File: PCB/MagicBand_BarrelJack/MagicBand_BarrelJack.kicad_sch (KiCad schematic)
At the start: 18 parts, among them J2 MFRC522_Module, J3 RF_TX_DFLIFE, J6 NeoPixel_Outer_16px, J7 NeoPixel_Inner_12px, J8 DC_Barrel_Jack_5.5x2.1mm, J9 ISP_AVR_2x3, U1 ATmega328P-P, U2 MCP1700-3302, Y1 16MHz

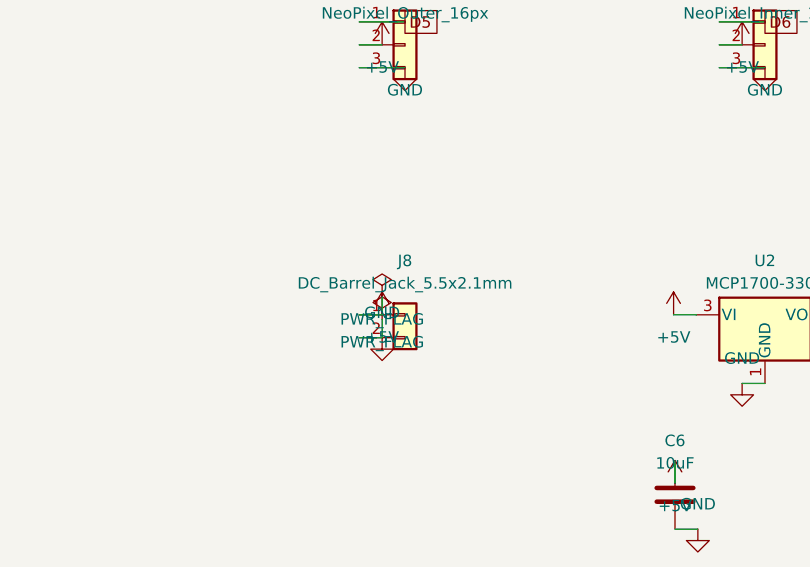
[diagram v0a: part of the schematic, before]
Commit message: Document front/back layout constraint, relabel barrel jack connector
RFID+MCU stack must sit at the front (interactive/tap end) of the
ornament; the barrel jack must be at the back. The jack itself is a
separate panel-mount part with bare flying leads, not board-mounted --
it connects to the board via two soldered wires, not a purchased
connector. Relabeled J8 to PWR_IN_BarrelJack_BareLeads to make that
explicit, and added a Physical Layout Constraint section to the PCB
Design Plan so this isn't missed once actual placement/routing starts.
ERC re-run clean, no regression.

Co-Authored-By: Claude Sonnet 5 <noreply@anthropic.com>
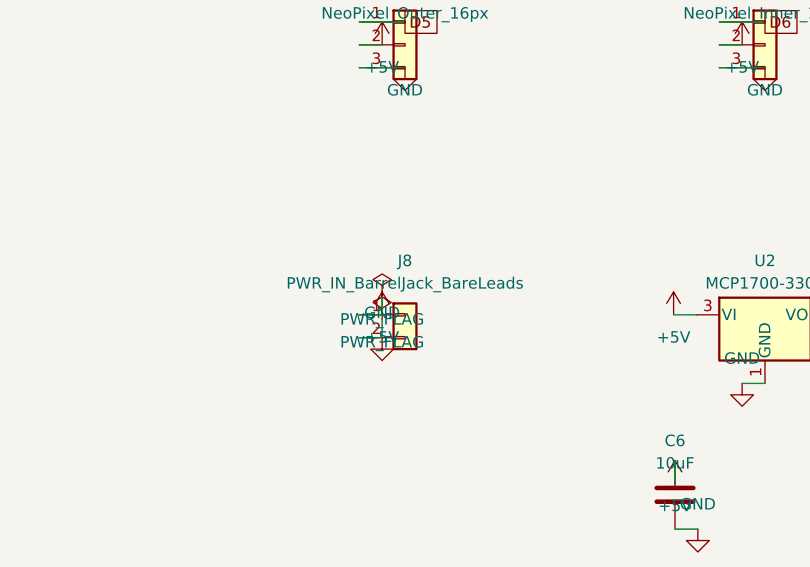
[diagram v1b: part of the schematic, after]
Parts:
- J8: value DC_Barrel_Jack_5.5x2.1mm -> PWR_IN_BarrelJack_BareLeads
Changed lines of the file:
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@@
 			(effects (font (size 1.27 1.27)))
 		)
-		(property "Value" "DC_Barrel_Jack_5.5x2.1mm"
+		(property "Value" "PWR_IN_BarrelJack_BareLeads"
 			(at 250 126.5 0)
 			(effects (font (size 1.27 1.27)))

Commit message: NeoPixel headers: JST-PH connector, pin order documented
J6/J7 changed from generic 2.54mm pin headers to JST-PH 3-pin connectors
for easier connect/disconnect at assembly. Pin order (1=DATA, 2=+5V,
3=GND) confirmed identical on both headers via netlist before the swap,
and documented in PCB Design Plan.md since there's no external standard
JST pin order for WS2812 strips to rely on -- the user is terminating
both ends themselves, so this table is the source of truth.

J3 (RF TX module) shares the same generic footprint family and was
deliberately left untouched -- caught by an assertion check before the
replacement ran, not something that would have been obvious from a
find-and-replace alone.

ERC re-run clean, no regression (0 errors, 194 warnings).

Co-Authored-By: Claude Sonnet 5 <noreply@anthropic.com>
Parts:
- J6, J7: footprint Connector_PinHeader_2.54mm:PinHeader_1x03_P2.54mm_Vertical -> Connector_JST:JST_PH_B3B-PH-K_1x03_P2.00mm_Vertical
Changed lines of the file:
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@@
 			(effects (font (size 1.27 1.27)))
 		)
-		(property "Footprint" "Connector_PinHeader_2.54mm:PinHeader_1x03_P2.54mm_Vertical"
+		(property "Footprint" "Connector_JST:JST_PH_B3B-PH-K_1x03_P2.00mm_Vertical"
 			(at 250 100 0)
 			(effects (font (size 1.27 1.27)) (hide yes))
@@
 			(effects (font (size 1.27 1.27)))
 		)
-		(property "Footprint" "Connector_PinHeader_2.54mm:PinHeader_1x03_P2.54mm_Vertical"
+		(property "Footprint" "Connector_JST:JST_PH_B3B-PH-K_1x03_P2.00mm_Vertical"
 			(at 290 100 0)
 			(effects (font (size 1.27 1.27)) (hide yes))

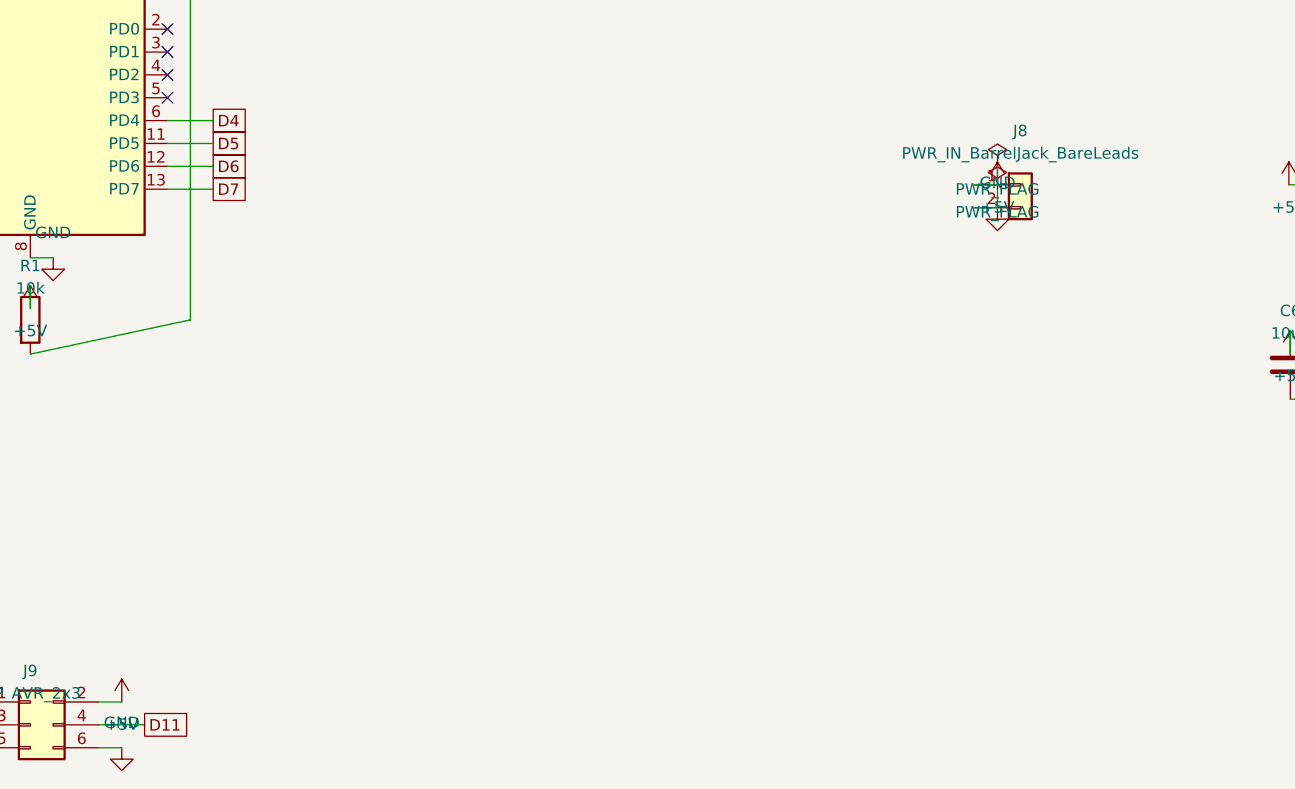
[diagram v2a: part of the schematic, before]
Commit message: Close PDR gaps: reverse-polarity protection, firmware trim, cleanup
Adversarial PDR found one blocking issue and five should-fix items on
PCB/MagicBand_BarrelJack/MagicBand_BarrelJack.kicad_sch. All closed:

- Blocking: added a P-channel MOSFET (Q1, AO3401A) ideal-diode
  reverse-polarity protection circuit ahead of the regulator/MCU -- the
  barrel jack is bare wire leads with no mechanical keying, a real risk
  of a reversed or wrong-voltage adapter with nothing previously in the
  way. MOSFET chosen over a simple diode to avoid eating into the
  ATmega328P's 16MHz voltage headroom. Topology cross-checked against
  real references before committing. ERC-clean (0 errors, 209 warnings)
  after fixing real geometry/connectivity issues hit while authoring it.

- Should-fix: removed an orphaned D7 label (explicit no-connect added),
  linked the front/back layout constraint into the WP4.1 task text,
  documented the MFRC522/ISP shared-SPI-bus gotcha, made the MCP1700-keep
  decision explicit, fixed a doc typo (SOT-23-5 -> SOT-23).

- Firmware: new MagicBand_BarrelJack.ino, derived from
  MagicBand_Wireless.ino with the sleep/wake watchdog loop and MOSFET
  gating calls removed -- the leftover ~1s poll delay was a real UX
  regression, not just stale code. Compiles clean.

Co-Authored-By: Claude Sonnet 5 <noreply@anthropic.com>
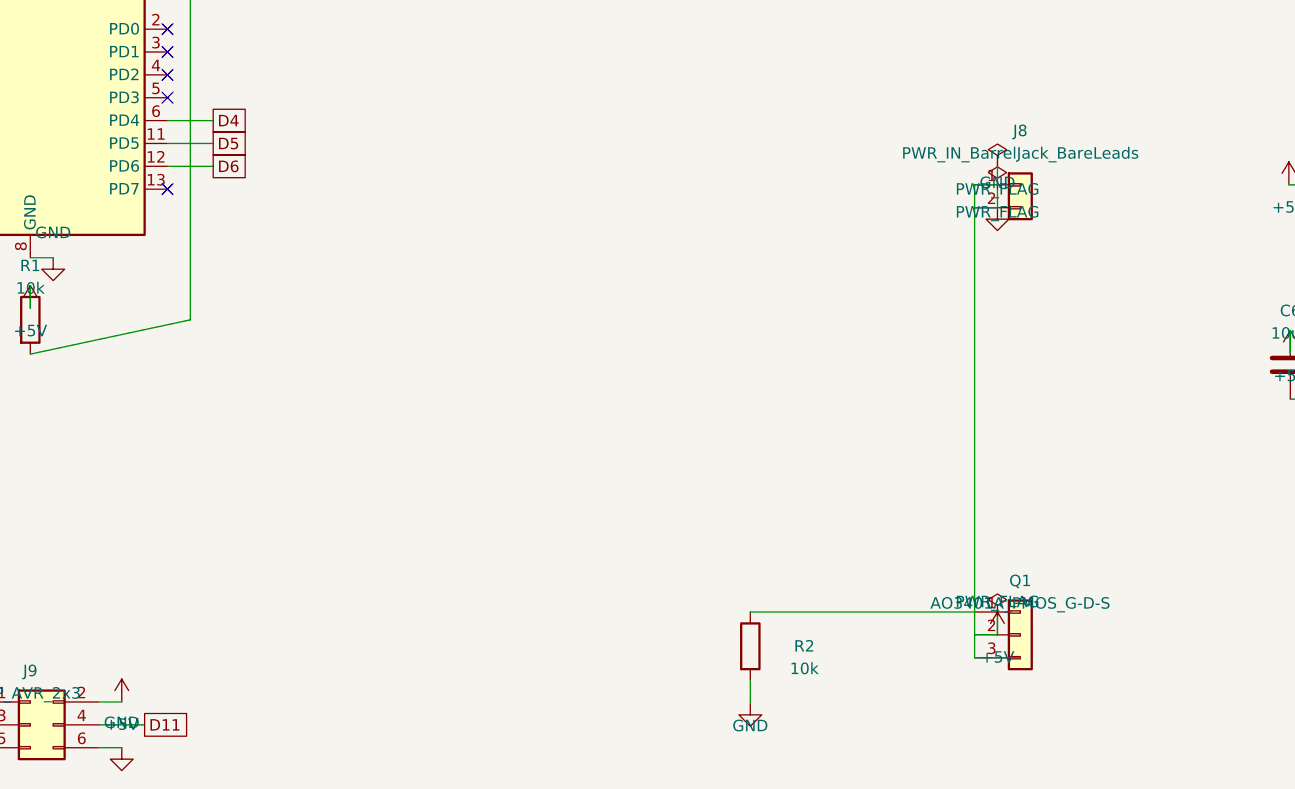
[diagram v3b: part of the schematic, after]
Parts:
- added Q1: AO3401A_PMOS_G-D-S, Package_TO_SOT_SMD:SOT-23, symbol Connector_Generic:Conn_01x03
- added R2: 10k, Resistor_THT:R_Axial_DIN0207_L6.3mm_D2.5mm_P10.16mm_Horizontal, symbol Device:R
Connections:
- net +5V: now also Q1.2 (Pin_2); no longer J8.1 (Pin_1)
- net GND: now also R2.2
- net D7: no longer names the net of U1.13 (PD7)
- new net: J8.1 (Pin_1), Q1.3 (Pin_3)
- new net: Q1.1 (Pin_1), R2.1
- no-connect marks 12 -> 13
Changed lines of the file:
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@@
-	)
-	(wire
-		(pts (xy 155.24 130.48) (xy 160.32 130.48))
-		(stroke (width 0) (type default))
-	)
-	(global_label "D7"
-		(shape passive)
-		(at 160.32 130.48 0)
-		(fields_autoplaced yes)
-		(effects (font (size 1.27 1.27)) (justify left))
 	)
 	(wire
@@
 	(no_connect (at 155.24 120.32))
 	(no_connect (at 155.24 74.6))
+	(no_connect (at 155.24 130.48))
 	(no_connect (at 155.24 92.38))
 	(no_connect (at 155.24 94.92))
@@
 	)
 	(wire
+		(pts (xy 244.92 130.0) (xy 244.92 182.54))
+		(stroke (width 0) (type default))
+	)
+	(wire
 		(pts (xy 244.92 130.0) (xy 247.45999999999998 130.0))
 		(stroke (width 0) (type default))
 	)
+	(wire
+		(pts (xy 244.92 182.54) (xy 250 182.54))
+		(stroke (width 0) (type default))
+	)
+	(symbol
+		(lib_id "Connector_Generic:Conn_01x03")
+		(at 250 180 0)
+		(unit 1)
+		(exclude_from_sim no)
+		(in_bom yes)
+		(on_board yes)
+		(dnp no)
+		(property "Reference" "Q1"
+			(at 250 174 0)
+			(effects (font (size 1.27 1.27)))
+		)
+		(property "Value" "AO3401A_PMOS_G-D-S"
+			(at 250 176.5 0)
+			(effects (font (size 1.27 1.27)))
+		)
+		(property "Footprint" "Package_TO_SOT_SMD:SOT-23"
+			(at 250 180 0)
+			(effects (font (size 1.27 1.27)) (hide yes))
+		)
+		(property "Datasheet" ""
+			(at 250 180 0)
+			(effects (font (size 1.27 1.27)) (hide yes))
+		)
+		(pin "1")
+		(pin "2")
+		(pin "3")
+		(instances
+			(project "MagicBand_BarrelJack"
+				(path "/bcfef247-dfd6-4ae3-b42f-2bc22ccfcf8a"
+					(reference "Q1")
+					(unit 1)
+				)
+			)
+		)
+	)
+	(wire
+		(pts (xy 220 177.46) (xy 244.92 177.46))
+		(stroke (width 0) (type default))
+	)
+	(wire
+		(pts (xy 244.92 180.0) (xy 247.46 180.0))
+		(stroke (width 0) (type default))
+	)
 	(symbol
 		(lib_id "power:+5V")
-		(at 247.45999999999998 130.0 0)
-		(unit 1)
-		(exclude_from_sim no)
-		(in_bom yes)
-		(on_board yes)
-		(dnp no)
-		(property "Reference" "#PWR459d"
-			(at 247.45999999999998 126.5 0)
+		(at 247.46 180.0 0)
+		(unit 1)
+		(exclude_from_sim no)
+		(in_bom yes)
+		(on_board yes)
+		(dnp no)
+		(property "Reference" "#PWRQ1D"
+			(at 247.46 176.5 0)
 			(effects (font (size 1.27 1.27)) (hide yes))
 		)
 		(property "Value" "+5V"
-			(at 247.45999999999998 132.5 0)
-			(effects (font (size 1.27 1.27)))
-		)
-		(property "Footprint" ""
-			(at 247.45999999999998 130.0 0)
-			(effects (font (size 1.27 1.27)) (hide yes))
-		)
-		(property "Datasheet" ""
-			(at 247.45999999999998 130.0 0)
-			(effects (font (size 1.27 1.27)) (hide yes))
-		)
-		(pin "1")
-		(instances
-			(project "MagicBand_BarrelJack"
-				(path "/bcfef247-dfd6-4ae3-b42f-2bc22ccfcf8a"
-					(reference "#PWR459d")
-					(unit 1)
-				)
+			(at 247.46 182.5 0)
+			(effects (font (size 1.27 1.27)))
+		)
+		(property "Footprint" ""
+			(at 247.46 180.0 0)
+			(effects (font (size 1.27 1.27)) (hide yes))
+		)
+		(property "Datasheet" ""
+			(at 247.46 180.0 0)
+			(effects (font (size 1.27 1.27)) (hide yes))
+		)
+		(pin "1")
+		(instances
+			(project "MagicBand_BarrelJack"
+				(path "/bcfef247-dfd6-4ae3-b42f-2bc22ccfcf8a"
+					(reference "#PWRQ1D")
+					(unit 1)
+				)
+			)
+		)
+	)
+	(wire
+		(pts (xy 247.46 180.0) (xy 247.46 178.0))
+		(stroke (width 0) (type default))
+	)
+	(symbol
+		(lib_id "power:PWR_FLAG")
+		(at 247.46 178.0 0)
+		(unit 1)
+		(exclude_from_sim no)
+		(in_bom yes)
+		(on_board yes)
+		(dnp no)
+		(property "Reference" "#FLGQ1D"
+			(at 247.46 174.5 0)
+			(effects (font (size 1.27 1.27)) (hide yes))
+		)
+		(property "Value" "PWR_FLAG"
+			(at 247.46 176.34 0)
+			(effects (font (size 1.27 1.27)))
+		)
+		(property "Footprint" ""
+			(at 247.46 178.0 0)
+			(effects (font (size 1.27 1.27)) (hide yes))
+		)
+		(property "Datasheet" ""
+			(at 247.46 178.0 0)
+			(effects (font (size 1.27 1.27)) (hide yes))
+		)
+		(pin "1")
+		(instances
+			(project "MagicBand_BarrelJack"
+				(path "/bcfef247-dfd6-4ae3-b42f-2bc22ccfcf8a"
+					(reference "#FLGQ1D")
+					(unit 1)
+				)
+			)
+		)
+	)
+	(symbol
+		(lib_id "Device:R")
+		(at 220 181.27 0)
+		(unit 1)
+		(exclude_from_sim no)
+		(in_bom yes)
+		(on_board yes)
+		(dnp no)
+		(property "Reference" "R2"
+			(at 226 181.27 0)
+			(effects (font (size 1.27 1.27)))
+		)
+		(property "Value" "10k"
+			(at 226 183.77 0)
+			(effects (font (size 1.27 1.27)))
+		)
+		(property "Footprint" "Resistor_THT:R_Axial_DIN0207_L6.3mm_D2.5mm_P10.16mm_Horizontal"
+			(at 220 181.27 0)
+			(effects (font (size 1.27 1.27)) (hide yes))
+		)
+		(property "Datasheet" ""
+			(at 220 181.27 0)
+			(effects (font (size 1.27 1.27)) (hide yes))
+		)
+		(pin "1")
+		(pin "2")
+		(instances
+			(project "MagicBand_BarrelJack"
+				(path "/bcfef247-dfd6-4ae3-b42f-2bc22ccfcf8a"
+					(reference "R2")
+					(unit 1)
+				)
+			)
+		)
+	)
+	(wire
+		(pts (xy 220 185.08) (xy 220 187.62))
+		(stroke (width 0) (type default))
+	)
+	(symbol
+		(lib_id "power:GND")
+		(at 220 187.62 0)
+		(unit 1)
+		(exclude_from_sim no)
+		(in_bom yes)
+		(on_board yes)
+		(dnp no)
+		(property "Reference" "#PWRQ1G"
+			(at 220 184.12 0)
+			(effects (font (size 1.27 1.27)) (hide yes))
+		)
+		(property "Value" "GND"
+			(at 220 190.12 0)
+			(effects (font (size 1.27 1.27)))
+		)
+		(property "Footprint" ""
+			(at 220 187.62 0)
+			(effects (font (size 1.27 1.27)) (hide yes))
+		)
+		(property "Datasheet" ""
+			(at 220 187.62 0)
+			(effects (font (size 1.27 1.27)) (hide yes))
+		)
+		(pin "1")
+		(instances
+			(project "MagicBand_BarrelJack"
+				(path "/bcfef247-dfd6-4ae3-b42f-2bc22ccfcf8a"
+					(reference "#PWRQ1G")
+					(unit 1)
+				)

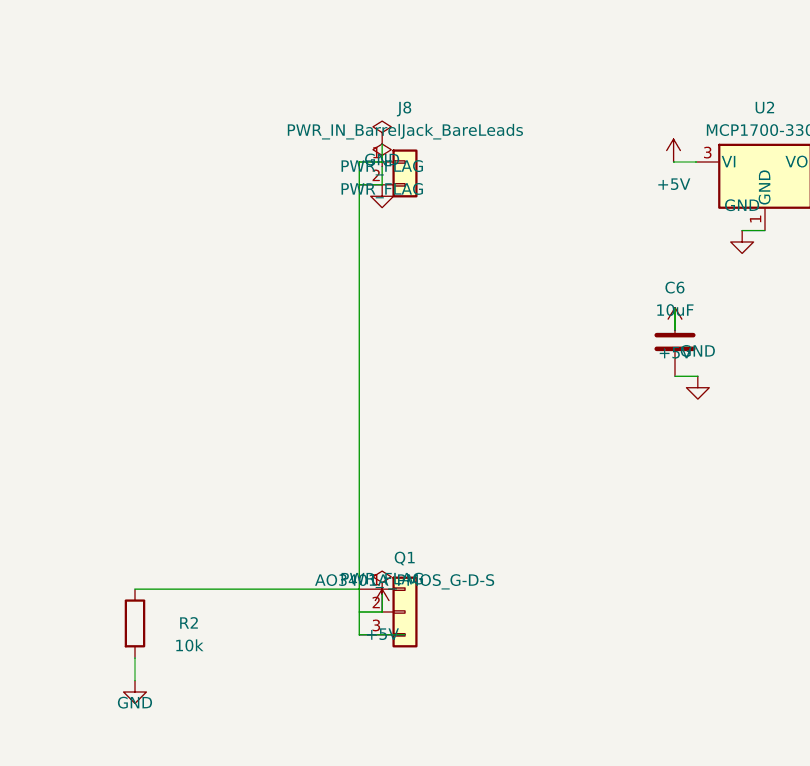
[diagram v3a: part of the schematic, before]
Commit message: Fix Q1 Source/Drain pin swap, close remaining review items
Second-round adversarial review found the reverse-polarity protection
MOSFET (Q1, AO3401A) wired backwards -- pin2 was treated as Drain, pin3
as Source, but the real part is Pin1=Gate/Pin2=Source/Pin3=Drain per
Alpha & Omega's own datasheet. Independently confirmed by rendering the
actual datasheet PDF locally and reading the pin diagram directly (not
trusting any prior claim). As wired, the circuit likely would not have
functioned -- possibly blocking power even under correct polarity.

Fixed by swapping which net lands on pins 2/3, verified via netlist
export before and after (ERC alone can't catch this class of bug).
ERC clean, no regression: 0 errors, 209 warnings.

Also closed two remaining minor items: two more stale SOT-23-5 doc
references, and a 50ms idle delay added to the firmware's polling loop
(was running the MFRC522 through zero-gap continuous power-cycling).

Co-Authored-By: Claude Sonnet 5 <noreply@anthropic.com>
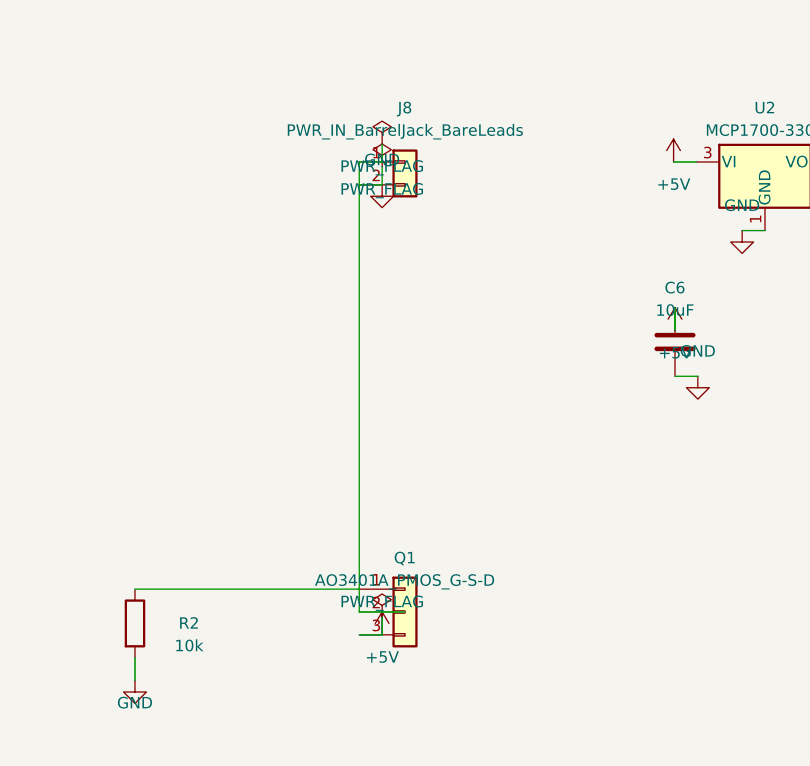
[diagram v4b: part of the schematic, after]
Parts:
- Q1: value AO3401A_PMOS_G-D-S -> AO3401A_PMOS_G-S-D
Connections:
- net +5V: now also Q1.3 (Pin_3); no longer Q1.2 (Pin_2)
- net at J8.1 (Pin_1): now also Q1.2 (Pin_2); no longer Q1.3 (Pin_3)
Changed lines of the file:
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@@
 	)
 	(wire
-		(pts (xy 244.92 130.0) (xy 244.92 182.54))
+		(pts (xy 244.92 130.0) (xy 244.92 180.0))
 		(stroke (width 0) (type default))
 	)
@@
 	)
 	(wire
-		(pts (xy 244.92 182.54) (xy 250 182.54))
+		(pts (xy 244.92 180.0) (xy 250 180.0))
 		(stroke (width 0) (type default))
 	)
@@
 			(effects (font (size 1.27 1.27)))
 		)
-		(property "Value" "AO3401A_PMOS_G-D-S"
+		(property "Value" "AO3401A_PMOS_G-S-D"
 			(at 250 176.5 0)
 			(effects (font (size 1.27 1.27)))
@@
 	)
 	(wire
-		(pts (xy 244.92 180.0) (xy 247.46 180.0))
+		(pts (xy 244.92 182.54) (xy 247.46 182.54))
 		(stroke (width 0) (type default))
 	)
 	(symbol
 		(lib_id "power:+5V")
-		(at 247.46 180.0 0)
+		(at 247.46 182.54 0)
 		(unit 1)
 		(exclude_from_sim no)
@@
 		(dnp no)
 		(property "Reference" "#PWRQ1D"
-			(at 247.46 176.5 0)
+			(at 247.46 179.04 0)
 			(effects (font (size 1.27 1.27)) (hide yes))
 		)
 		(property "Value" "+5V"
-			(at 247.46 182.5 0)
+			(at 247.46 185.04 0)
 			(effects (font (size 1.27 1.27)))
 		)
 		(property "Footprint" ""
-			(at 247.46 180.0 0)
+			(at 247.46 182.54 0)
 			(effects (font (size 1.27 1.27)) (hide yes))
 		)
 		(property "Datasheet" ""
-			(at 247.46 180.0 0)
+			(at 247.46 182.54 0)
 			(effects (font (size 1.27 1.27)) (hide yes))
 		)
@@
 	)
 	(wire
-		(pts (xy 247.46 180.0) (xy 247.46 178.0))
+		(pts (xy 247.46 182.54) (xy 247.46 180.54))
 		(stroke (width 0) (type default))
 	)
 	(symbol
 		(lib_id "power:PWR_FLAG")
-		(at 247.46 178.0 0)
+		(at 247.46 180.54 0)
 		(unit 1)
 		(exclude_from_sim no)
@@
 		(dnp no)
 		(property "Reference" "#FLGQ1D"
-			(at 247.46 174.5 0)
+			(at 247.46 177.04 0)
 			(effects (font (size 1.27 1.27)) (hide yes))
 		)
 		(property "Value" "PWR_FLAG"
-			(at 247.46 176.34 0)
+			(at 247.46 178.88 0)
 			(effects (font (size 1.27 1.27)))
 		)
 		(property "Footprint" ""
-			(at 247.46 178.0 0)
+			(at 247.46 180.54 0)
 			(effects (font (size 1.27 1.27)) (hide yes))
 		)
 		(property "Datasheet" ""
-			(at 247.46 178.0 0)
+			(at 247.46 180.54 0)
 			(effects (font (size 1.27 1.27)) (hide yes))
 		)
